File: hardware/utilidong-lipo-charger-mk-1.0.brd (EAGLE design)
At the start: 24 x 22 mm, 16 parts, among them Q1 N-MOSFET, U1 MCP73831

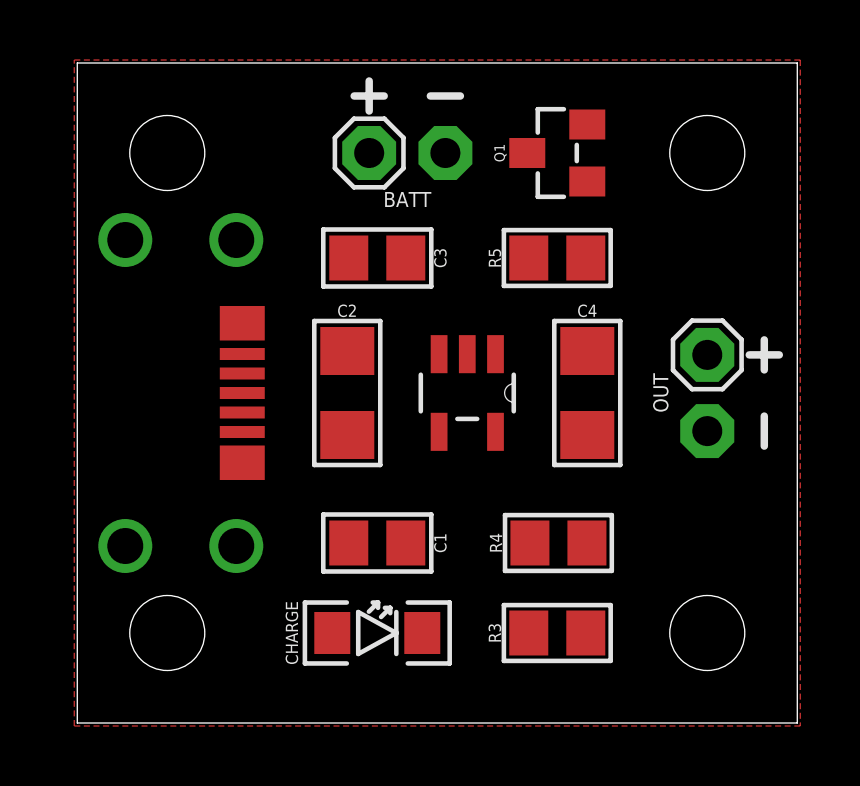
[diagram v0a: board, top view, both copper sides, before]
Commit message: stand-alone usb lipo charger
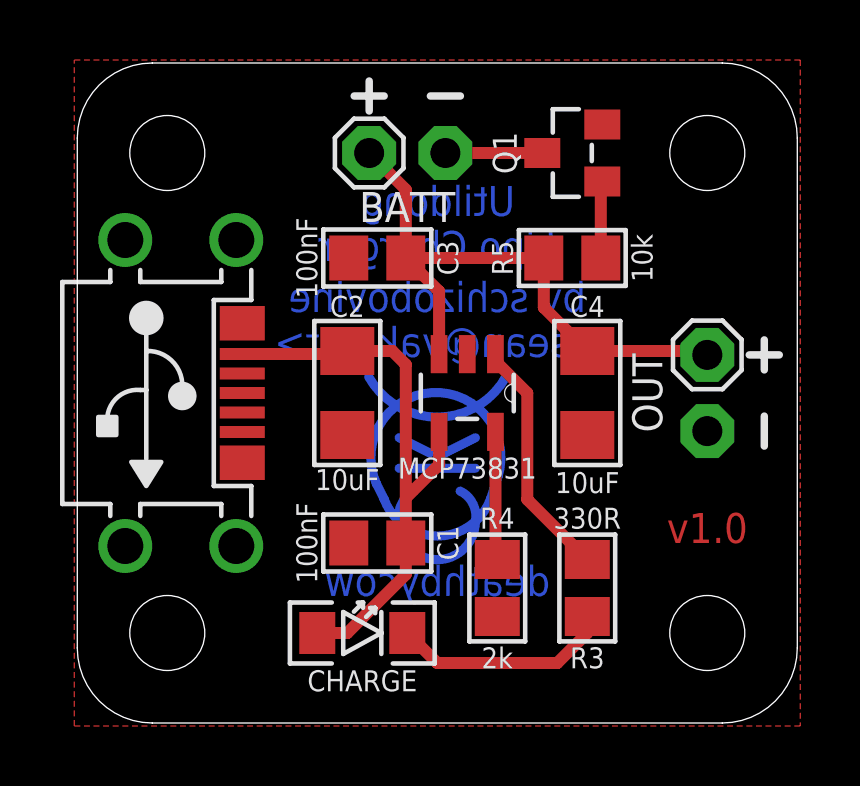
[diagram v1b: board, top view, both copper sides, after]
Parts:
- removed U$7: (no value), A_butts:COW_SMALL
- added U$9: (no value), A_butts:COW_SMALL_METAL
- moved U$8 23.3 mm to (12.0, 2.00), turned to 0 degrees
- moved R4 2.53 mm to (14.0, 4.50), turned to 270 degrees
- moved R3 1.80 mm to (17.0, 4.50), turned to 90 degrees
- moved CHARGE 0.50 mm to (9.50, 3.00)
- moved Q1 0.50 mm to (16.5, 19.0)
- moved R5 0.50 mm to (16.5, 15.5)
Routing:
- net VBATT+: track 0.00 -> 20.0 mm
- net 5V: track 0.00 -> 19.1 mm
- net N$5: track 0.00 -> 8.11 mm
- net N$6: track 0.00 -> 7.38 mm
- net N$8: track 0.00 -> 4.49 mm
- net VBATT-: track 0.00 -> 3.23 mm
- net N$11: track 0.00 -> 2.57 mm
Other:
- outline, holes or cut-outs redrawn
- board text added: ">VERSION"
